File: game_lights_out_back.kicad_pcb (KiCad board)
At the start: 2 copper layers, 171 x 127.3 mm, 5 parts

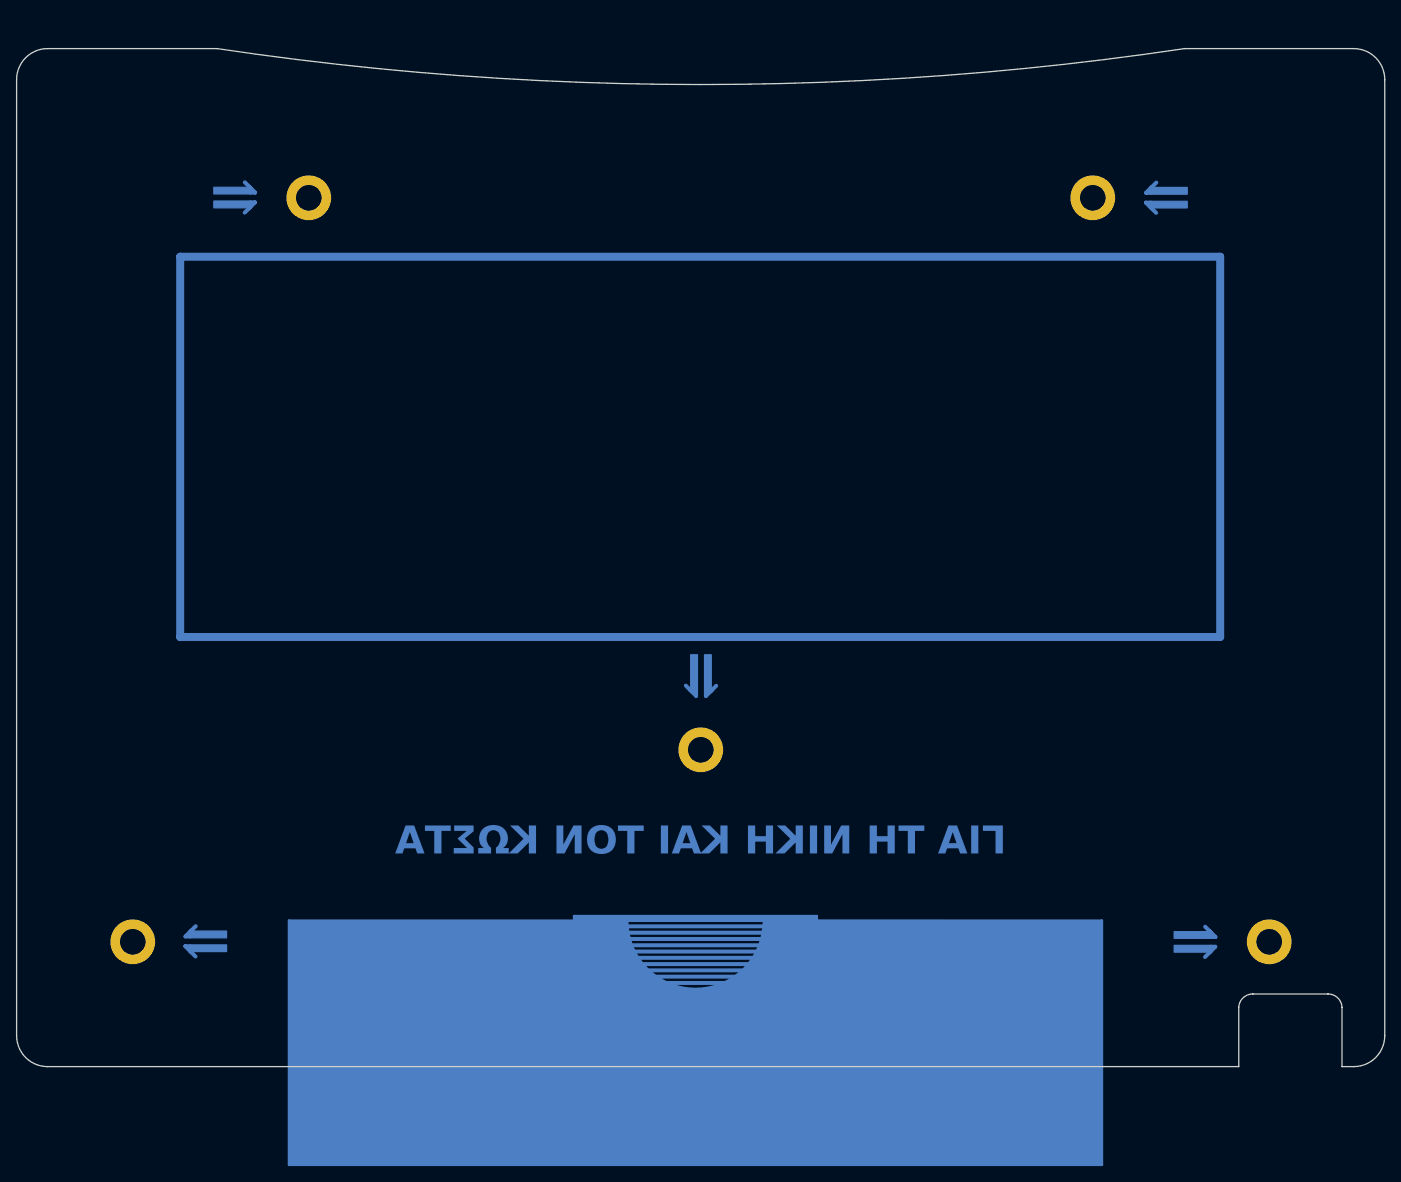
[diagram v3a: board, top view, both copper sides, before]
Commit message: Added order number placeholder
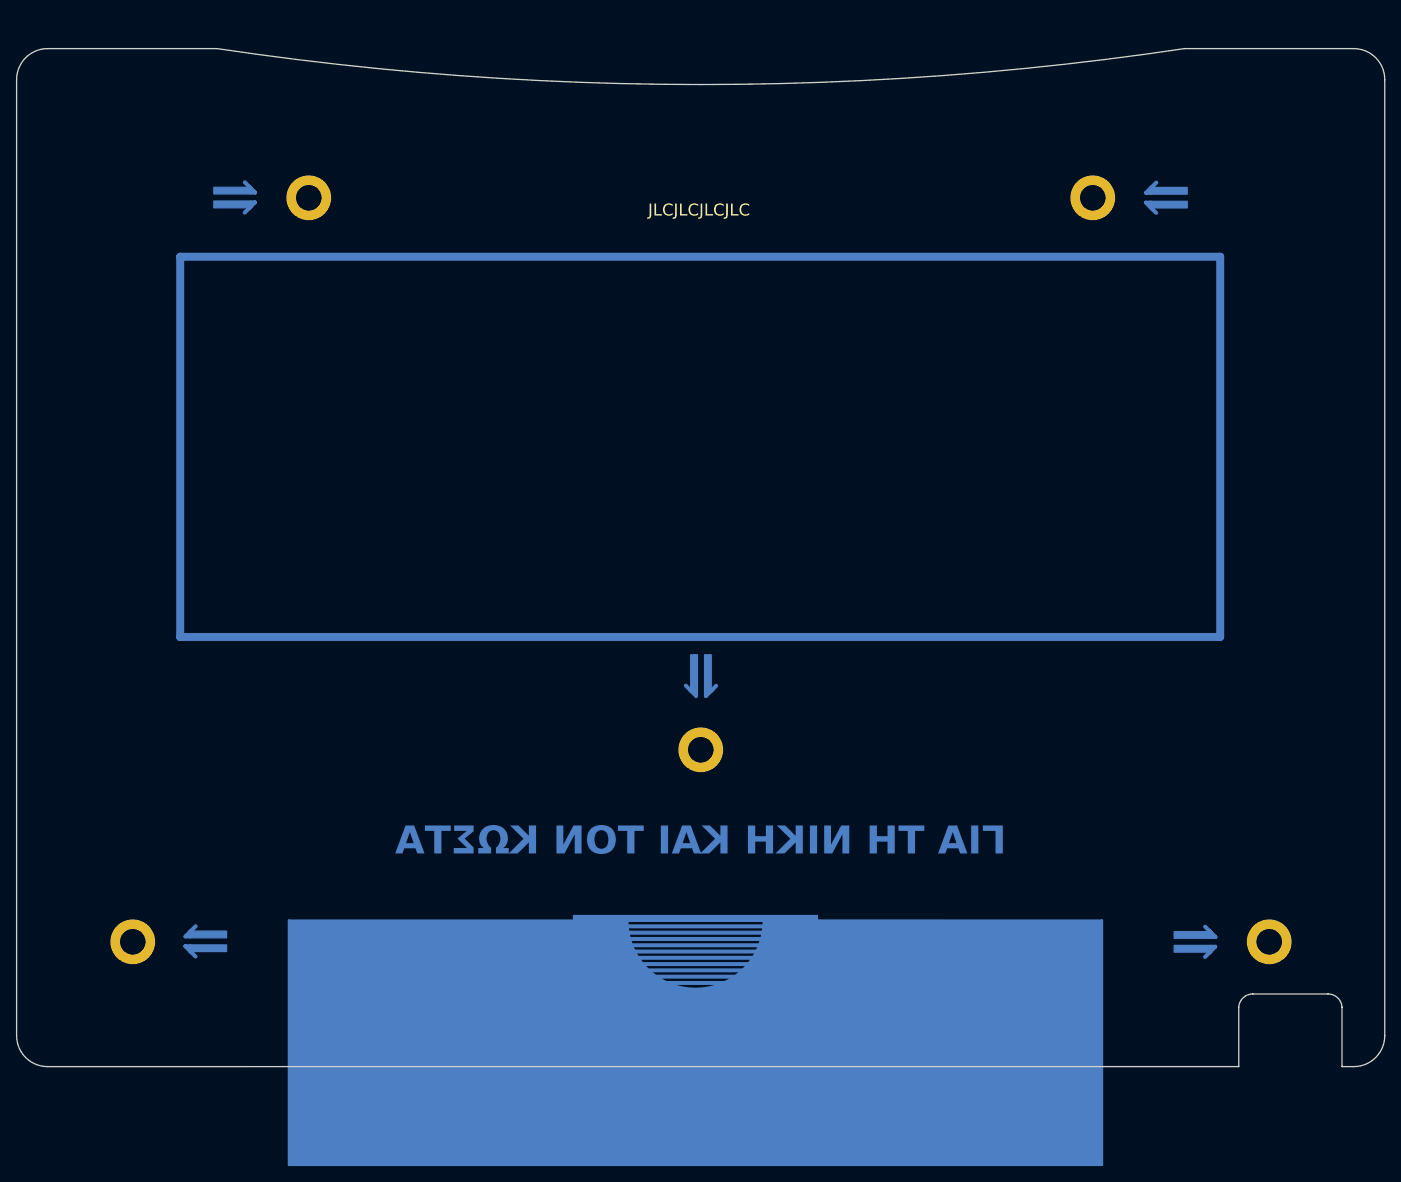
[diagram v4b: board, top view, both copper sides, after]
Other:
- board text added: "JLCJLCJLCJLC"
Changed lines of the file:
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@@
   (gr_line (start 168.67 54.3752) (end 169.27 54.3752)
     (stroke (width 0.5) (type default)) (layer "B.Cu"))
-  (gr_rect (start 53.73 149.225) (end 49.055 148.3846)
+  (gr_rect (start 49.055 148.3846) (end 53.73 149.225)
     (stroke (width 0.15) (type default)) (fill solid) (layer "B.Cu"))
   (gr_line (start 169.23 53.8152) (end 169.95 53.0952)
@@
   (gr_line (start 113.6452 117.28) (end 113.6452 116.68)
     (stroke (width 0.5) (type default)) (layer "B.Cu"))
-  (gr_rect (start 173.81 56.2702) (end 169.135 55.4298)
+  (gr_rect (start 169.135 55.4298) (end 173.81 56.2702)
     (stroke (width 0.15) (type default)) (fill solid) (layer "B.Cu"))
   (gr_line (start 48.59 147.33) (end 49.19 147.33)
     (stroke (width 0.5) (type default)) (layer "B.Cu"))
-  (gr_rect (start 112.5904 112.12) (end 111.74 116.795)
+  (gr_rect (start 111.74 112.12) (end 112.5904 116.795)
     (stroke (width 0.15) (type default)) (fill solid) (layer "B.Cu"))
   (gr_line (start 48.57 148.56) (end 49.17 148.56)
@@
   (gr_line (start 177.33 147.39) (end 176.73 147.39)
     (stroke (width 0.5) (type default)) (layer "B.Cu"))
-  (gr_rect (start 173.81 54.5504) (end 169.135 53.7)
-    (stroke (width 0.15) (type default)) (fill solid) (layer "B.Cu"))
-  (gr_rect (start 114.3102 112.12) (end 113.4698 116.795)
-    (stroke (width 0.15) (type default)) (fill solid) (layer "B.Cu"))
-  (gr_rect (start 53.73 147.5052) (end 49.055 146.6548)
+  (gr_rect (start 169.135 53.7) (end 173.81 54.5504)
+    (stroke (width 0.15) (type default)) (fill solid) (layer "B.Cu"))
+  (gr_rect (start 113.4698 112.12) (end 114.3102 116.795)
+    (stroke (width 0.15) (type default)) (fill solid) (layer "B.Cu"))
+  (gr_rect (start 49.055 146.6548) (end 53.73 147.5052)
     (stroke (width 0.15) (type default)) (fill solid) (layer "B.Cu"))
   (gr_line (start 119.2125 150.787775) (end 105.5625 150.787775)
@@
     (effects (font (size 3 3) (thickness 0.4)) (justify left bottom mirror))
   )
+  (gr_text "JLCJLCJLCJLC" (at 112.785 56.525) (layer "F.SilkS")
+    (effects (font (size 1.5 1.5) (thickness 0.2)))
+  )
   (group "" (id 455a1178-df87-44ea-8b91-7235553cbc28)
